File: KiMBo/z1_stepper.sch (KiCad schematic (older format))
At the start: 23 parts, among them U21 TMC2130

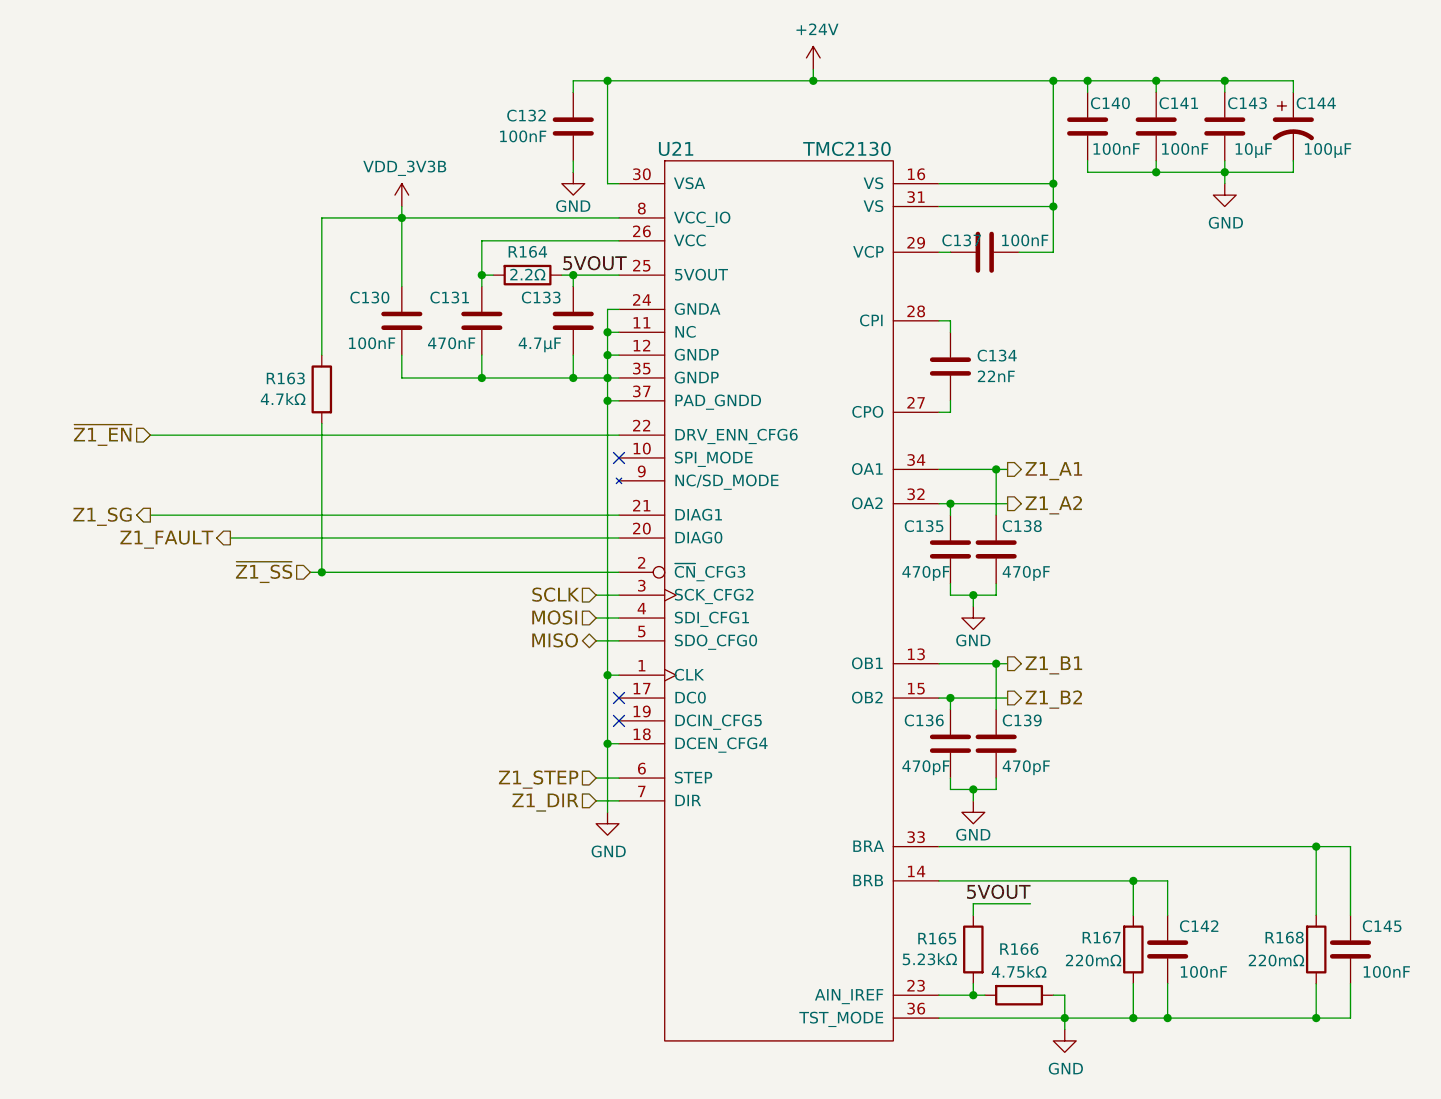
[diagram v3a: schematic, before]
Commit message: Begin layout
Arrange all connectors to get a feel for the area.
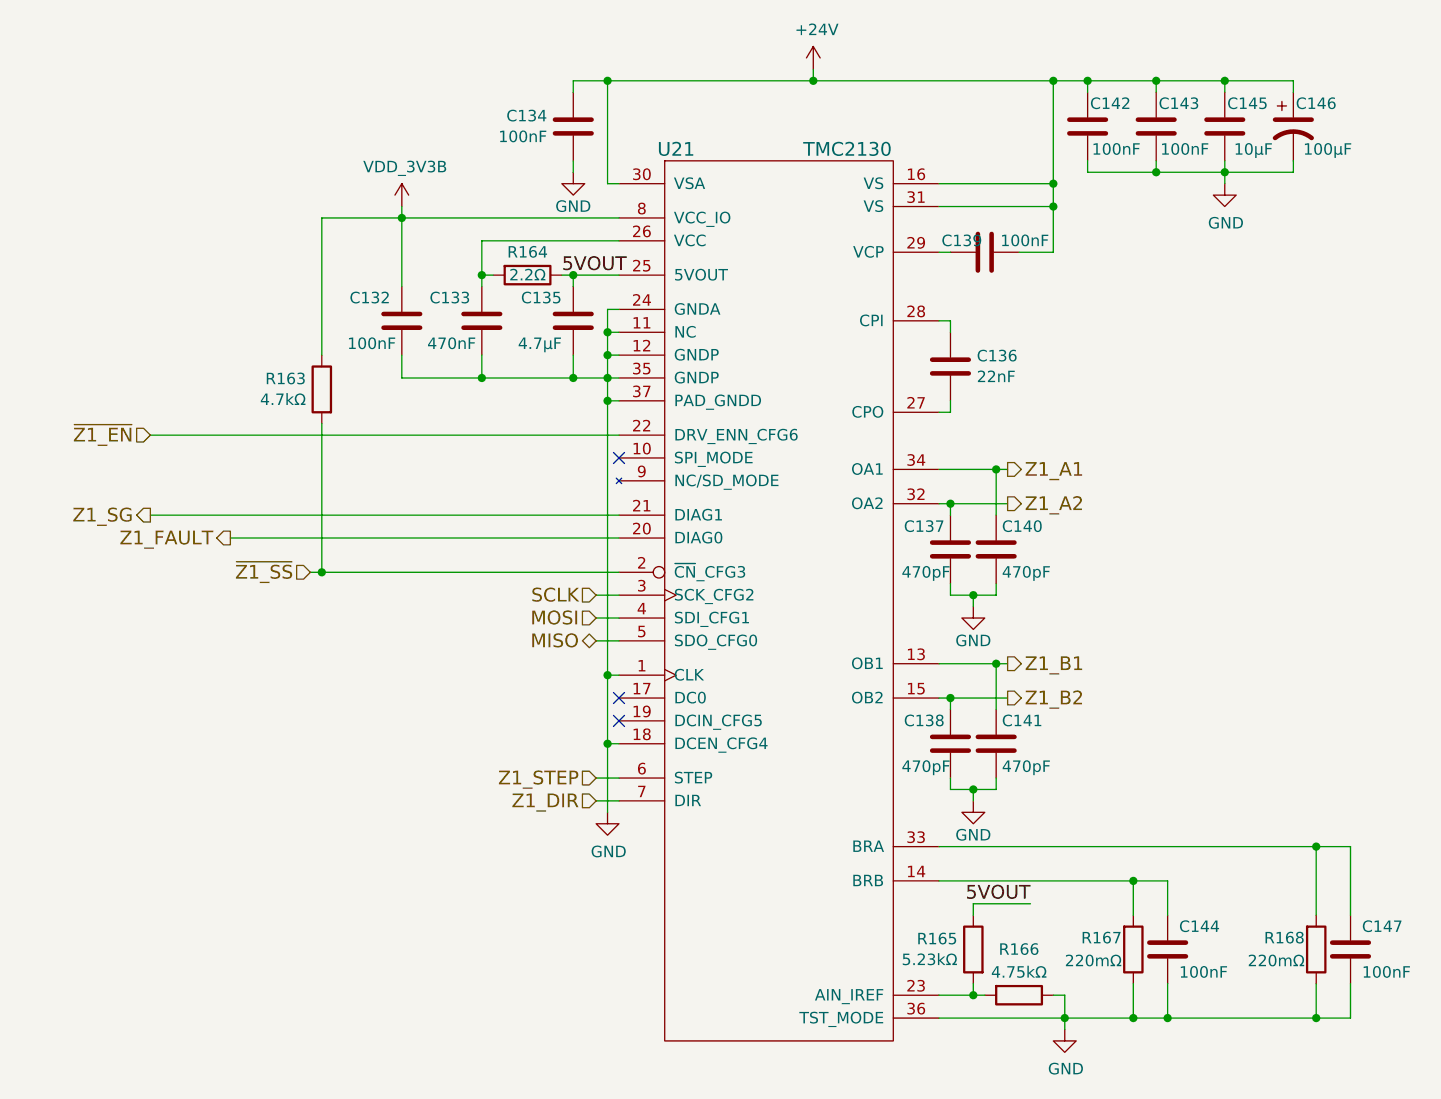
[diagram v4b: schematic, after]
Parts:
- renumbered C130 to C132, C131 to C133, C132 to C134, C133 to C135, C134 to C136, C135 to C137, C136 to C138, C137 to C139, C138 to C140, C139 to C141, C140 to C142, C141 to C143, C142 to C144, C143 to C145, C144 to C146, C145 to C147
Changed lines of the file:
@@
 Z1_SG
 $Comp
-L C C132
+L C C134
 U 1 1 58C0CFD1
 P 7400 3050
-F 0 "C132" H 7286 3004 50  0000 R CNN
+F 0 "C134" H 7286 3004 50  0000 R CNN
 F 1 "100nF" H 7286 3095 50  0000 R CNN
 F 2 "Capacitors_SMD:C_0603" H 7438 2900 50  0001 C CNN
@@
 $EndComp
 $Comp
-L C C137
+L C C139
 U 1 1 58C0CFD8
 P 9200 3600
-F 0 "C137" V 9150 3500 50  0000 C CNN
+F 0 "C139" V 9150 3500 50  0000 C CNN
 F 1 "100nF" V 9150 3775 50  0000 C CNN
 F 2 "Capacitors_SMD:C_0603" H 9238 3450 50  0001 C CNN
@@
 $EndComp
 $Comp
-L CP1 C144
+L CP1 C146
 U 1 1 58C0CFDF
 P 10550 3050
-F 0 "C144" H 10650 3150 50  0000 C CNN
+F 0 "C146" H 10650 3150 50  0000 C CNN
 F 1 "100μF" H 10700 2950 50  0000 C CNN
 F 2 "Capacitors_SMD:c_elec_8x10" H 10550 3050 50  0001 C CNN
@@
 $EndComp
 $Comp
-L C C140
+L C C142
 U 1 1 58C0CFE6
 P 9650 3050
-F 0 "C140" H 9550 3150 50  0000 C CNN
+F 0 "C142" H 9550 3150 50  0000 C CNN
 F 1 "100nF" H 9525 2950 50  0000 C CNN
 F 2 "Capacitors_SMD:C_0603" H 9688 2900 50  0001 C CNN
@@
 $EndComp
 $Comp
-L GND #PWR0221
+L GND #PWR0224
 U 1 1 58C0CFED
 P 7400 3250
-F 0 "#PWR0221" H 7400 3000 50  0001 C CNN
+F 0 "#PWR0224" H 7400 3000 50  0001 C CNN
 F 1 "GND" H 7400 3100 50  0000 C CNN
 F 2 "" H 7400 3250 50  0000 C CNN
@@
 $EndComp
 $Comp
-L C C141
+L C C143
 U 1 1 58C0CFF3
 P 9950 3050
-F 0 "C141" H 9850 3150 50  0000 C CNN
+F 0 "C143" H 9850 3150 50  0000 C CNN
 F 1 "100nF" H 9825 2950 50  0000 C CNN
 F 2 "Capacitors_SMD:C_0603" H 9988 2900 50  0001 C CNN
@@
 $EndComp
 $Comp
-L GND #PWR0222
+L GND #PWR0225
 U 1 1 58C0CFFA
 P 10250 3300
-F 0 "#PWR0222" H 10250 3050 50  0001 C CNN
+F 0 "#PWR0225" H 10250 3050 50  0001 C CNN
 F 1 "GND" H 10255 3127 50  0000 C CNN
 F 2 "" H 10250 3300 50  0000 C CNN
@@
 $EndComp
 $Comp
-L +24V #PWR0223
+L +24V #PWR0226
 U 1 1 58C0D000
 P 8450 2800
-F 0 "#PWR0223" H 8450 2650 50  0001 C CNN
+F 0 "#PWR0226" H 8450 2650 50  0001 C CNN
 F 1 "+24V" H 8465 2973 50  0000 C CNN
 F 2 "" H 8450 2800 50  0000 C CNN
@@
 $EndComp
 $Comp
-L C C134
+L C C136
 U 1 1 58C0D006
 P 9050 4100
-F 0 "C134" H 9165 4146 50  0000 L CNN
+F 0 "C136" H 9165 4146 50  0000 L CNN
 F 1 "22nF" H 9165 4055 50  0000 L CNN
 F 2 "Capacitors_SMD:C_0603" H 9088 3950 50  0001 C CNN
@@
 $EndComp
 $Comp
-L GND #PWR0224
+L GND #PWR0227
 U 1 1 58C0D01B
 P 9550 7000
-F 0 "#PWR0224" H 9550 6750 50  0001 C CNN
+F 0 "#PWR0227" H 9550 6750 50  0001 C CNN
 F 1 "GND" H 9555 6827 50  0000 C CNN
 F 2 "" H 9550 7000 50  0000 C CNN
@@
 $EndComp
 $Comp
-L C C131
+L C C133
 U 1 1 58C0D029
 P 7000 3900
-F 0 "C131" H 7050 4000 50  0000 L CNN
+F 0 "C133" H 7050 4000 50  0000 L CNN
 F 1 "470nF" H 7025 3800 50  0000 L CNN
 F 2 "Capacitors_SMD:C_0603" H 7038 3750 50  0001 C CNN
@@
 NoConn ~ 7600 5650
 $Comp
-L GND #PWR0225
+L GND #PWR0228
 U 1 1 58C0D03E
 P 7550 6050
-F 0 "#PWR0225" H 7550 5800 50  0001 C CNN
+F 0 "#PWR0228" H 7550 5800 50  0001 C CNN
 F 1 "GND" H 7555 5877 50  0000 C CNN
 F 2 "" H 7550 6050 50  0000 C CNN
@@
 $EndComp
 $Comp
-L C C142
+L C C144
 U 1 1 58C0D044
 P 10000 6650
-F 0 "C142" H 10050 6750 50  0000 L CNN
+F 0 "C144" H 10050 6750 50  0000 L CNN
 F 1 "100nF" H 10050 6550 50  0000 L CNN
 F 2 "Capacitors_SMD:C_0603" H 10038 6500 50  0001 C CNN
@@
 NoConn ~ 7600 4500
 $Comp
-L C C133
+L C C135
 U 1 1 58C0D056
 P 7400 3900
-F 0 "C133" H 7450 4000 50  0000 L CNN
+F 0 "C135" H 7450 4000 50  0000 L CNN
 F 1 "4.7μF" H 7450 3800 50  0000 L CNN
 F 2 "Capacitors_SMD:C_0603" H 7438 3750 50  0001 C CNN
@@
 $EndComp
 $Comp
-L C C145
+L C C147
 U 1 1 58C0D074
 P 10800 6650
-F 0 "C145" H 10850 6750 50  0000 L CNN
+F 0 "C147" H 10850 6750 50  0000 L CNN
 F 1 "100nF" H 10850 6550 50  0000 L CNN
 F 2 "Capacitors_SMD:C_0603" H 10838 6500 50  0001 C CNN
@@
 $EndComp
 $Comp
-L C C135
+L C C137
 U 1 1 58C0D07B
 P 9050 4900
-F 0 "C135" H 9075 5000 50  0000 L CNN
+F 0 "C137" H 9075 5000 50  0000 L CNN
 F 1 "470pF" H 9050 4800 50  0000 L CNN
 F 2 "Capacitors_SMD:C_0603" H 9088 4750 50  0001 C CNN
@@
 $EndComp
 $Comp
-L GND #PWR0226
+L GND #PWR0229
 U 1 1 58C0D082
 P 9150 5150
-F 0 "#PWR0226" H 9150 4900 50  0001 C CNN
+F 0 "#PWR0229" H 9150 4900 50  0001 C CNN
 F 1 "GND" H 9150 5000 50  0000 C CNN
 F 2 "" H 9150 5150 50  0000 C CNN
@@
 $EndComp
 $Comp
-L C C138
+L C C140
 U 1 1 58C0D088
 P 9250 4900
-F 0 "C138" H 9275 5000 50  0000 L CNN
+F 0 "C140" H 9275 5000 50  0000 L CNN
 F 1 "470pF" H 9275 4800 50  0000 L CNN
 F 2 "Capacitors_SMD:C_0603" H 9288 4750 50  0001 C CNN
@@
 $EndComp
 $Comp
-L C C136
+L C C138
 U 1 1 58C0D08F
 P 9050 5750
-F 0 "C136" H 9075 5850 50  0000 L CNN
+F 0 "C138" H 9075 5850 50  0000 L CNN
 F 1 "470pF" H 9050 5650 50  0000 L CNN
 F 2 "Capacitors_SMD:C_0603" H 9088 5600 50  0001 C CNN
@@
 $EndComp
 $Comp
-L GND #PWR0227
+L GND #PWR0230
 U 1 1 58C0D096
 P 9150 6000
-F 0 "#PWR0227" H 9150 5750 50  0001 C CNN
+F 0 "#PWR0230" H 9150 5750 50  0001 C CNN
 F 1 "GND" H 9150 5850 50  0000 C CNN
 F 2 "" H 9150 6000 50  0000 C CNN
@@
 $EndComp
 $Comp
-L C C139
+L C C141
 U 1 1 58C0D09C
 P 9250 5750
-F 0 "C139" H 9275 5850 50  0000 L CNN
+F 0 "C141" H 9275 5850 50  0000 L CNN
 F 1 "470pF" H 9275 5650 50  0000 L CNN
 F 2 "Capacitors_SMD:C_0603" H 9288 5600 50  0001 C CNN
@@
 	9050 5950 9050 5900
 $Comp
-L C C143
+L C C145
 U 1 1 58C0D122
 P 10250 3050
-F 0 "C143" H 10150 3150 50  0000 C CNN
+F 0 "C145" H 10150 3150 50  0000 C CNN
 F 1 "10μF" H 10125 2950 50  0000 C CNN
 F 2 "Capacitors_SMD:C_0805" H 10288 2900 50  0001 C CNN
@@
 	9000 4550 9300 4550
 $Comp
-L VDD_3V3B #PWR0228
+L VDD_3V3B #PWR0231
 U 1 1 5A314607
 P 6650 3400
-F 0 "#PWR0228" H 6650 3250 50  0001 C CNN
+F 0 "#PWR0231" H 6650 3250 50  0001 C CNN
 F 1 "VDD_3V3B" H 6665 3573 50  0000 C CNN
 F 2 "" H 6650 3400 50  0000 C CNN
@@
 $EndComp
 $Comp
-L C C130
+L C C132
 U 1 1 5A89C1CC
 P 6650 3900
-F 0 "C130" H 6700 4000 50  0000 L CNN
+F 0 "C132" H 6700 4000 50  0000 L CNN
 F 1 "100nF" H 6675 3800 50  0000 L CNN
 F 2 "Capacitors_SMD:C_0603" H 6688 3750 50  0001 C CNN

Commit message: Arrange connectors and E-stepper circuit
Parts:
- R166: footprint Resistors_SMD:R_0805 -> Resistors_SMD:R_0603
- R168: footprint Resistors_SMD:R_0603 -> Resistors_SMD:R_0805
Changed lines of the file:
@@
 F 0 "R168" H 10600 6600 50  0000 R CNN
 F 1 "220mΩ" H 10600 6700 50  0000 R CNN
-F 2 "Resistors_SMD:R_0603" V 10580 6650 50  0001 C CNN
+F 2 "Resistors_SMD:R_0805" V 10580 6650 50  0001 C CNN
 F 3 "" H 10650 6650 50  0000 C CNN
 	1    10650 6650
@@
 F 0 "R166" V 9150 6850 50  0000 C CNN
 F 1 "4.75kΩ" V 9250 6850 50  0000 C CNN
-F 2 "Resistors_SMD:R_0805" V 9280 6850 50  0001 C CNN
+F 2 "Resistors_SMD:R_0603" V 9280 6850 50  0001 C CNN
 F 3 "" H 9350 6850 50  0000 C CNN
 	1    9350 6850
